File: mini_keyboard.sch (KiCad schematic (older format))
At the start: 42 parts, among them SW1 SW_DIP_x01, SW10 SW_DIP_x01, SW11 SW_DIP_x01, SW12 SW_DIP_x01, SW13 SW_DIP_x01, SW14 SW_DIP_x01, SW15 SW_DIP_x01, SW16 SW_DIP_x01, SW17 SW_DIP_x01, SW18 SW_DIP_x01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

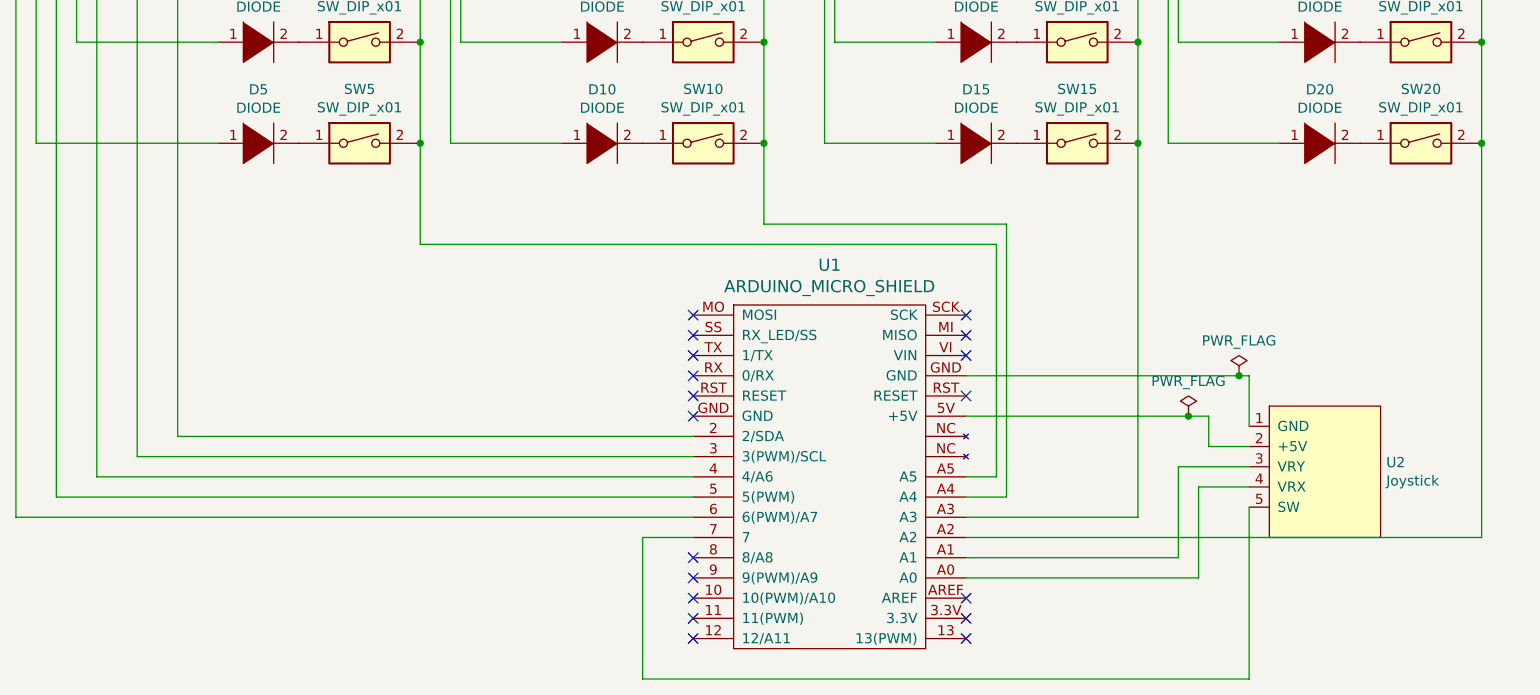
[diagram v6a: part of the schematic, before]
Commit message: pro micro + pin for joystick
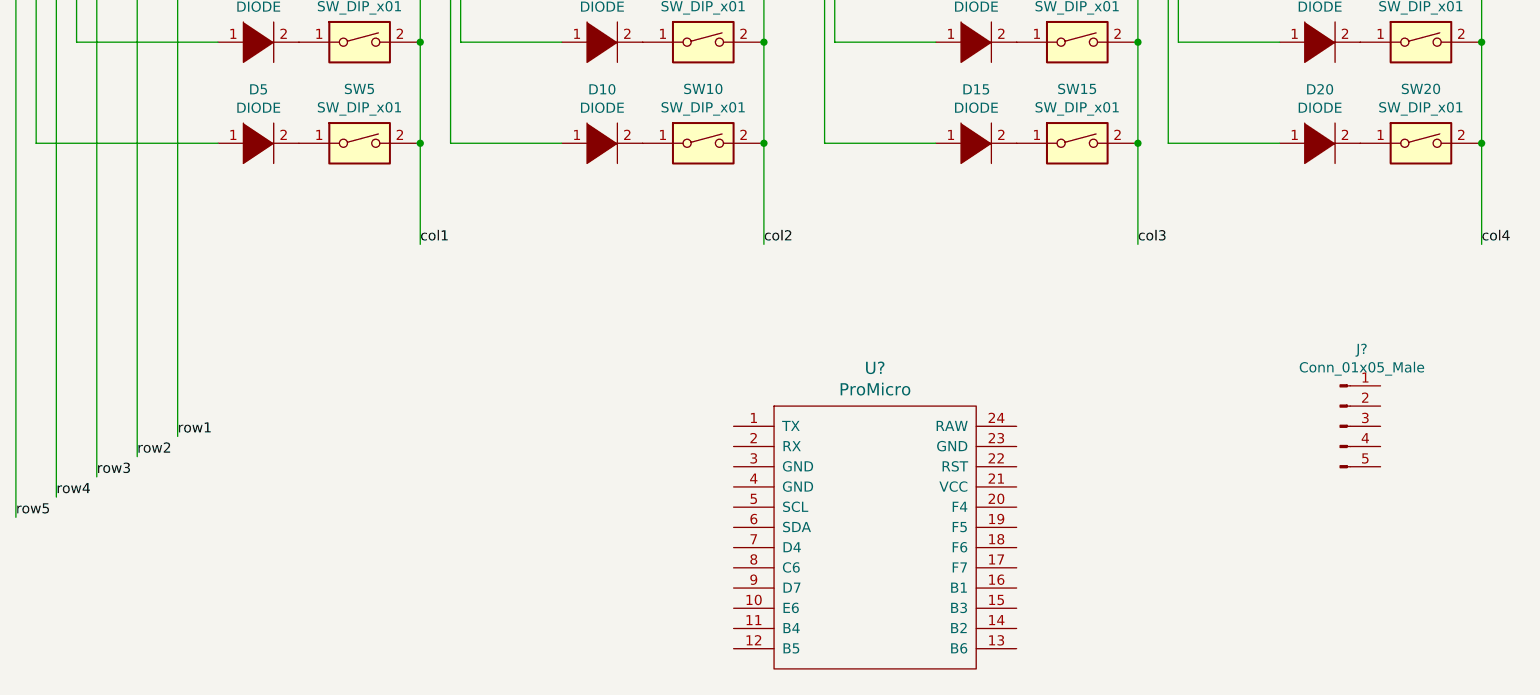
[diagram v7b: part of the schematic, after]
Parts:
- removed U1: ARDUINO_MICRO_SHIELD, arduino_micro_shield:ARDUINO_MICRO_SHIELD, symbol arduino_micro_shield:ARDUINO_MICRO_SHIELD
- removed U2: Joystick, Joystick:Joystick, symbol mini_keyboard-rescue:Joystick-joystick
- added J?: Conn_01x05_Male, symbol Connector:Conn_01x05_Male
- added U?: ProMicro, symbol promicro:ProMicro
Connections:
- net row1: now reaches D1.1 (K), D11.1 (K), D16.1 (K), D6.1 (K)
- net row2: now reaches D12.1 (K), D17.1 (K), D2.1 (K), D7.1 (K)
- net row3: now reaches D13.1 (K), D18.1 (K), D3.1 (K), D8.1 (K)
- net row4: now reaches D14.1 (K), D19.1 (K), D4.1 (K), D9.1 (K)
- net row5: now reaches D10.1 (K), D15.1 (K), D20.1 (K), D5.1 (K)
- net col4: now reaches SW16.2, SW17.2, SW18.2, SW19.2, SW20.2
- net col3: now reaches SW11.2, SW12.2, SW13.2, SW14.2, SW15.2
- net col2: now reaches SW10.2, SW6.2, SW7.2, SW8.2, SW9.2
- net col1: now reaches SW1.2, SW2.2, SW3.2, SW4.2, SW5.2
- no-connect marks 18 -> 0
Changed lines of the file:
@@
 Comment4 ""
 $EndDescr
-NoConn ~ 5000 6700
-NoConn ~ 6350 6700
-NoConn ~ 6350 6600
-NoConn ~ 6350 6500
-NoConn ~ 6350 5500
-NoConn ~ 6350 5300
-NoConn ~ 6350 5200
-NoConn ~ 6350 5100
 $Comp
 L Switch:SW_DIP_x01 SW12
@@
 $EndComp
 $Comp
-L arduino_micro_shield:ARDUINO_MICRO_SHIELD U1
-U 1 1 5FD3DC77
-P 5200 5050
-F 0 "U1" V 5003 5525 60  0000 C CNN
-F 1 "ARDUINO_MICRO_SHIELD" V 5109 5525 60  0000 C CNN
-F 2 "arduino_micro_shield:ARDUINO_MICRO_SHIELD" H 5600 5000 60  0001 C CNN
-F 3 "" H 5600 5000 60  0000 C CNN
-	1    5200 5050
-	0    1    1    0
-$EndComp
-NoConn ~ 5000 6600
-NoConn ~ 5000 6500
-NoConn ~ 5000 6400
-NoConn ~ 5000 6300
-NoConn ~ 5000 5100
-NoConn ~ 5000 5200
-NoConn ~ 5000 5300
-NoConn ~ 5000 5400
-NoConn ~ 5000 5500
-$Comp
 L pspice:DIODE D13
 U 1 1 5FD9DB0A
@@
 $EndComp
 Wire Wire Line
-	5000 5700 2450 5700
-Wire Wire Line
-	5000 5800 2250 5800
-Wire Wire Line
 	7700 2700 7900 2700
 Wire Wire Line
@@
 	2350 2700 2650 2700
 Wire Wire Line
-	5000 5900 2050 5900
-Wire Wire Line
 	2050 5900 2050 1200
 Wire Wire Line
@@
 Wire Wire Line
 	1850 6000 1850 900
-Wire Wire Line
-	1850 6000 5000 6000
 Wire Wire Line
 	1850 900  1950 900
@@
 Connection ~ 3650 3250
 Wire Wire Line
-	3650 4750 6500 4750
-Wire Wire Line
-	6500 4750 6500 5900
-Wire Wire Line
-	6500 5900 6350 5900
-Wire Wire Line
 	5350 2700 5350 3250
 Wire Wire Line
@@
 Connection ~ 5350 3250
 Wire Wire Line
-	6550 4650 6550 6000
-Wire Wire Line
-	6550 6000 6350 6000
-Wire Wire Line
 	7200 2700 7200 3250
 Wire Wire Line
@@
 Connection ~ 7200 3250
 Wire Wire Line
-	7200 6100 6350 6100
-Wire Wire Line
 	8900 2250 8900 2700
 Wire Wire Line
@@
 	8900 3250 8900 3750
 Connection ~ 8900 3250
-Wire Wire Line
-	8900 6200 6350 6200
 $Comp
 L Switch:SW_DIP_x01 SW5
@@
 Connection ~ 8900 3750
 Wire Wire Line
-	8900 6200 8900 4250
-Connection ~ 8900 4250
-Wire Wire Line
 	7200 3750 7200 4250
 Connection ~ 7200 3750
-Wire Wire Line
-	7200 4250 7200 6100
-Connection ~ 7200 4250
-Wire Wire Line
-	5350 4650 6550 4650
 $Comp
 L Switch:SW_DIP_x01 SW10
@@
 Connection ~ 5350 3750
 Wire Wire Line
-	5350 4250 5350 4650
-Connection ~ 5350 4250
-Wire Wire Line
 	3650 3750 3650 4250
 Connection ~ 3650 3750
 Wire Wire Line
-	3650 4750 3650 4250
-Connection ~ 3650 4250
-Wire Wire Line
-	5000 6100 1650 6100
-Wire Wire Line
 	1650 6100 1650 650
 Wire Wire Line
@@
 Wire Wire Line
 	1750 4250 1750 650
-Wire Wire Line
-	7550 5600 7550 5750
-Wire Wire Line
-	7400 5850 7400 6300
-Wire Wire Line
-	7400 6300 6350 6300
-Wire Wire Line
-	6350 6400 7500 6400
-Wire Wire Line
-	7500 6400 7500 5950
-Wire Wire Line
-	7750 6900 4750 6900
-Wire Wire Line
-	4750 6900 4750 6200
-Wire Wire Line
-	4750 6200 5000 6200
-Wire Wire Line
-	7750 5850 7400 5850
-Wire Wire Line
-	7500 5950 7750 5950
-Wire Wire Line
-	7750 6050 7750 6900
-Wire Wire Line
-	7750 5400 7750 5650
-$Comp
-L mini_keyboard-rescue:Joystick-joystick U2
-U 1 1 5FD914AC
-P 8100 5900
-F 0 "U2" H 8428 5971 50  0000 L CNN
-F 1 "Joystick" H 8428 5880 50  0000 L CNN
-F 2 "Joystick:Joystick" H 8100 5900 50  0001 C CNN
-F 3 "" H 8100 5900 50  0001 C CNN
-	1    8100 5900
-	1    0    0    -1
-$EndComp
-NoConn ~ 5000 5600
-Wire Wire Line
-	7550 5750 7750 5750
-$Comp
-L power:PWR_FLAG #FLG0101
-U 1 1 5FFCD2BD
-P 7450 5600
-F 0 "#FLG0101" H 7450 5675 50  0001 C CNN
-F 1 "PWR_FLAG" H 7450 5773 50  0000 C CNN
-F 2 "" H 7450 5600 50  0001 C CNN
-F 3 "~" H 7450 5600 50  0001 C CNN
-	1    7450 5600
-	1    0    0    -1
-$EndComp
-Connection ~ 7450 5600
-Wire Wire Line
-	7450 5600 7550 5600
-Wire Wire Line
-	6350 5600 7450 5600
-$Comp
-L power:PWR_FLAG #FLG0102
-U 1 1 5FFD2873
-P 7700 5400
-F 0 "#FLG0102" H 7700 5475 50  0001 C CNN
-F 1 "PWR_FLAG" H 7700 5573 50  0000 C CNN
-F 2 "" H 7700 5400 50  0001 C CNN
-F 3 "~" H 7700 5400 50  0001 C CNN
-	1    7700 5400
-	1    0    0    -1
-$EndComp
-Wire Wire Line
-	6350 5400 7700 5400
-Connection ~ 7700 5400
-Wire Wire Line
-	7700 5400 7750 5400
 Connection ~ 1750 650
 Connection ~ 7200 2700
@@
 	1    0    0    -1
 $EndComp
+Text Label 2450 5700 0    50   ~ 0
+row1
+Text Label 2250 5800 0    50   ~ 0
+row2
+Text Label 2050 5900 0    50   ~ 0
+row3
+Text Label 1850 6000 0    50   ~ 0
+row4
+Text Label 1650 6100 0    50   ~ 0
+row5
+$Comp
+L promicro:ProMicro U?
+U 1 1 60148DE3
+P 5900 6400
+F 0 "U?" H 5900 7437 60  0000 C CNN
+F 1 "ProMicro" H 5900 7331 60  0000 C CNN
+F 2 "" H 6000 5350 60  0000 C CNN
+F 3 "" H 6000 5350 60  0000 C CNN
+	1    5900 6400
+	1    0    0    -1
+$EndComp
+Wire Wire Line
+	3650 4250 3650 4750
+Connection ~ 3650 4250
+Wire Wire Line
+	5350 4250 5350 4750
+Connection ~ 5350 4250
+Wire Wire Line
+	7200 4250 7200 4750
+Connection ~ 7200 4250
+Wire Wire Line
+	8900 4250 8900 4750
+Connection ~ 8900 4250
+Text Label 3650 4750 0    50   ~ 0
+col1
+Text Label 5350 4750 0    50   ~ 0
+col2
+Text Label 7200 4750 0    50   ~ 0
+col3
+Text Label 8900 4750 0    50   ~ 0
+col4
+$Comp
+L Connector:Conn_01x05_Male J?
+U 1 1 60183F68
+P 8200 5650
+F 0 "J?" H 8308 6031 50  0000 C CNN
+F 1 "Conn_01x05_Male" H 8308 5940 50  0000 C CNN
+F 2 "" H 8200 5650 50  0001 C CNN
+F 3 "~" H 8200 5650 50  0001 C CNN
+	1    8200 5650
+	1    0    0    -1
+$EndComp

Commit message: Added portal connections joystick
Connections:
- net col1: now also U?.20 (F4)
- net col2: now also U?.19 (F5)
- net col3: now also U?.18 (F6)
- net col4: now also U?.17 (F7)
- net row1: now also U?.5 (SCL)
- net row2: now also U?.6 (SDA)
- net row3: now also U?.7 (D4)
- net row4: now also U?.8 (C6)
- net row5: now also U?.9 (D7)
- net SW: now reaches J?.1 (Pin_1)
- net VRX: now reaches J?.2 (Pin_2)
- net VRY: now reaches J?.3 (Pin_3)
- net 5V: now reaches J?.4 (Pin_4)
- net GND: now reaches J?.5 (Pin_5)
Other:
- moved on the sheet: J?
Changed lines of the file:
@@
 Text Label 1650 6100 0    50   ~ 0
 row5
-$Comp
-L promicro:ProMicro U?
-U 1 1 60148DE3
-P 5900 6400
-F 0 "U?" H 5900 7437 60  0000 C CNN
-F 1 "ProMicro" H 5900 7331 60  0000 C CNN
-F 2 "" H 6000 5350 60  0000 C CNN
-F 3 "" H 6000 5350 60  0000 C CNN
-	1    5900 6400
-	1    0    0    -1
-$EndComp
 Wire Wire Line
 	3650 4250 3650 4750
@@
 L Connector:Conn_01x05_Male J?
 U 1 1 60183F68
-P 8200 5650
-F 0 "J?" H 8308 6031 50  0000 C CNN
-F 1 "Conn_01x05_Male" H 8308 5940 50  0000 C CNN
-F 2 "" H 8200 5650 50  0001 C CNN
-F 3 "~" H 8200 5650 50  0001 C CNN
-	1    8200 5650
+P 6000 7400
+F 0 "J?" H 6108 7781 50  0000 C CNN
+F 1 "Conn_01x05_Male" H 6108 7690 50  0000 C CNN
+F 2 "" H 6000 7400 50  0001 C CNN
+F 3 "~" H 6000 7400 50  0001 C CNN
+	1    6000 7400
+	0    -1   -1   0
+$EndComp
+$Comp
+L promicro:ProMicro U?
+U 1 1 60148DE3
+P 5900 6400
+F 0 "U?" H 5900 7437 60  0000 C CNN
+F 1 "ProMicro" H 5900 7331 60  0000 C CNN
+F 2 "" H 6000 5350 60  0000 C CNN
+F 3 "" H 6000 5350 60  0000 C CNN
+	1    5900 6400
 	1    0    0    -1
 $EndComp
+Text Label 6600 6050 0    50   ~ 0
+col1
+Text Label 6600 6150 0    50   ~ 0
+col2
+Text Label 6600 6250 0    50   ~ 0
+col3
+Text Label 6600 6350 0    50   ~ 0
+col4
+Text Label 5200 6050 2    50   ~ 0
+row1
+Text Label 5200 6150 2    50   ~ 0
+row2
+Text Label 5200 6250 2    50   ~ 0
+row3
+Text Label 5200 6350 2    50   ~ 0
+row4
+Text Label 5200 6450 2    50   ~ 0
+row5
+Text Label 6200 7200 1    50   ~ 0
+GND
+Text Label 6100 7200 1    50   ~ 0
+5V
+Text Label 6000 7200 1    50   ~ 0
+VRY
+Text Label 5900 7200 1    50   ~ 0
+VRX
+Text Label 5800 7200 1    50   ~ 0
+SW
 $EndSCHEMATC
